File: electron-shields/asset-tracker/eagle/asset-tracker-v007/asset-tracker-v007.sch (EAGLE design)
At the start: 45 parts, among them J1 1X2-3.5MM, Q1 MPSA42, T1 DMG3415, U1 MAX-M8, U3 LIS3DHTR, U4 RF_SWITCHSC-70-6, U5 SAFFB1G56KB0F0A, U6 BGA725L6-ALT, X1 ELECTRON, X2 IPEX-20279-001E

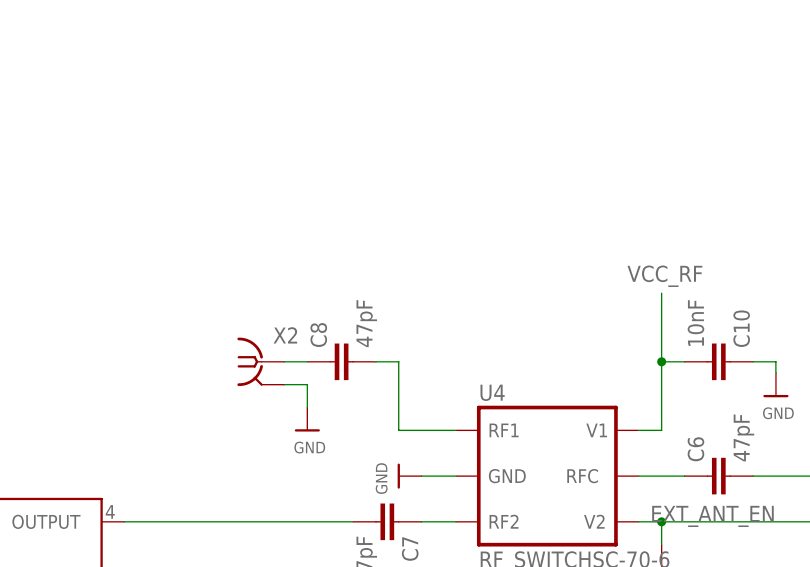
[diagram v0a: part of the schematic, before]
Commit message: added bias supply to the active antenna rf trace
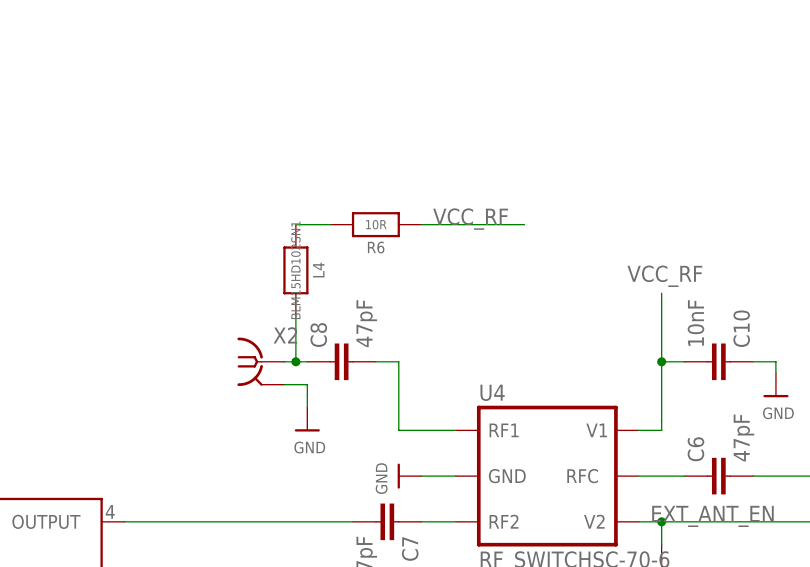
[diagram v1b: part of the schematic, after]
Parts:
- added L4: BLM15HD102SN1, microbuilder:RESISTOR_0402MP
- added R6: 10R, microbuilder:RESISTOR_0402MP
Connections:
- new net N$1: L4.1, R6.2
- net EXT_ANT: now also L4.2
- net VCC_RF: now also R6.1
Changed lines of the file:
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@@
 <setting verticaltext="up"/>
 </settings>
-<grid distance="0.1" unitdist="inch" unit="inch" style="lines" multiple="1" display="no" altdistance="0.01" altunitdist="inch" altunit="inch"/>
+<grid distance="0.05" unitdist="inch" unit="inch" style="lines" multiple="1" display="yes" altdistance="0.01" altunitdist="inch" altunit="inch"/>
 <layers>
-<layer number="1" name="Top" color="4" fill="1" visible="no" active="no"/>
-<layer number="2" name="Route2" color="5" fill="1" visible="no" active="no"/>
-<layer number="3" name="Route3" color="4" fill="3" visible="no" active="no"/>
-<layer number="4" name="Route4" color="1" fill="4" visible="no" active="no"/>
-<layer number="5" name="Route5" color="4" fill="4" visible="no" active="no"/>
-<layer number="6" name="Route6" color="1" fill="8" visible="no" active="no"/>
-<layer number="7" name="Route7" color="4" fill="8" visible="no" active="no"/>
-<layer number="8" name="Route8" color="1" fill="2" visible="no" active="no"/>
-<layer number="9" name="Route9" color="4" fill="2" visible="no" active="no"/>
-<layer number="10" name="Route10" color="1" fill="7" visible="no" active="no"/>
-<layer number="11" name="Route11" color="4" fill="7" visible="no" active="no"/>
-<layer number="12" name="Route12" color="1" fill="5" visible="no" active="no"/>
-<layer number="13" name="Route13" color="4" fill="5" visible="no" active="no"/>
-<layer number="14" name="Route14" color="1" fill="6" visible="no" active="no"/>
-<layer number="15" name="Route15" color="11" fill="1" visible="no" active="no"/>
-<layer number="16" name="Bottom" color="1" fill="1" visible="no" active="no"/>
-<layer number="17" name="Pads" color="2" fill="1" visible="no" active="no"/>
-<layer number="18" name="Vias" color="2" fill="1" visible="no" active="no"/>
-<layer number="19" name="Unrouted" color="6" fill="1" visible="no" active="no"/>
-<layer number="20" name="Dimension" color="15" fill="1" visible="no" active="no"/>
-<layer number="21" name="tPlace" color="16" fill="1" visible="no" active="no"/>
-<layer number="22" name="bPlace" color="14" fill="1" visible="no" active="no"/>
-<layer number="23" name="tOrigins" color="15" fill="1" visible="no" active="no"/>
-<layer number="24" name="bOrigins" color="15" fill="1" visible="no" active="no"/>
-<layer number="25" name="tNames" color="7" fill="1" visible="no" active="no"/>
-<layer number="26" name="bNames" color="7" fill="1" visible="no" active="no"/>
-<layer number="27" name="tValues" color="7" fill="1" visible="no" active="no"/>
-<layer number="28" name="bValues" color="7" fill="1" visible="no" active="no"/>
+<layer number="1" name="Top" color="4" fill="1" visible="yes" active="no"/>
+<layer number="2" name="Route2" color="5" fill="1" visible="yes" active="no"/>
+<layer number="3" name="Route3" color="4" fill="3" visible="yes" active="no"/>
+<layer number="4" name="Route4" color="1" fill="4" visible="yes" active="no"/>
+<layer number="5" name="Route5" color="4" fill="4" visible="yes" active="no"/>
+<layer number="6" name="Route6" color="1" fill="8" visible="yes" active="no"/>
+<layer number="7" name="Route7" color="4" fill="8" visible="yes" active="no"/>
+<layer number="8" name="Route8" color="1" fill="2" visible="yes" active="no"/>
+<layer number="9" name="Route9" color="4" fill="2" visible="yes" active="no"/>
+<layer number="10" name="Route10" color="1" fill="7" visible="yes" active="no"/>
+<layer number="11" name="Route11" color="4" fill="7" visible="yes" active="no"/>
+<layer number="12" name="Route12" color="1" fill="5" visible="yes" active="no"/>
+<layer number="13" name="Route13" color="4" fill="5" visible="yes" active="no"/>
+<layer number="14" name="Route14" color="1" fill="6" visible="yes" active="no"/>
+<layer number="15" name="Route15" color="11" fill="1" visible="yes" active="no"/>
+<layer number="16" name="Bottom" color="1" fill="1" visible="yes" active="no"/>
+<layer number="17" name="Pads" color="2" fill="1" visible="yes" active="no"/>
+<layer number="18" name="Vias" color="2" fill="1" visible="yes" active="no"/>
+<layer number="19" name="Unrouted" color="6" fill="1" visible="yes" active="no"/>
+<layer number="20" name="Dimension" color="15" fill="1" visible="yes" active="no"/>
+<layer number="21" name="tPlace" color="16" fill="1" visible="yes" active="no"/>
+<layer number="22" name="bPlace" color="14" fill="1" visible="yes" active="no"/>
+<layer number="23" name="tOrigins" color="15" fill="1" visible="yes" active="no"/>
+<layer number="24" name="bOrigins" color="15" fill="1" visible="yes" active="no"/>
+<layer number="25" name="tNames" color="7" fill="1" visible="yes" active="no"/>
+<layer number="26" name="bNames" color="7" fill="1" visible="yes" active="no"/>
+<layer number="27" name="tValues" color="7" fill="1" visible="yes" active="no"/>
+<layer number="28" name="bValues" color="7" fill="1" visible="yes" active="no"/>
 <layer number="29" name="tStop" color="32" fill="3" visible="no" active="no"/>
 <layer number="30" name="bStop" color="7" fill="6" visible="no" active="no"/>
@@
 <layer number="35" name="tGlue" color="7" fill="4" visible="no" active="no"/>
 <layer number="36" name="bGlue" color="7" fill="5" visible="no" active="no"/>
-<layer number="37" name="tTest" color="7" fill="1" visible="no" active="no"/>
-<layer number="38" name="bTest" color="7" fill="1" visible="no" active="no"/>
+<layer number="37" name="tTest" color="7" fill="1" visible="yes" active="no"/>
+<layer number="38" name="bTest" color="7" fill="1" visible="yes" active="no"/>
 <layer number="39" name="tKeepout" color="4" fill="11" visible="no" active="no"/>
 <layer number="40" name="bKeepout" color="1" fill="11" visible="no" active="no"/>
@@
 <layer number="44" name="Drills" color="7" fill="1" visible="no" active="no"/>
 <layer number="45" name="Holes" color="7" fill="1" visible="no" active="no"/>
-<layer number="46" name="Milling" color="3" fill="1" visible="no" active="no"/>
-<layer number="47" name="Measures" color="7" fill="1" visible="no" active="no"/>
-<layer number="48" name="Document" color="18" fill="1" visible="no" active="no"/>
-<layer number="49" name="Reference" color="17" fill="6" visible="no" active="no"/>
-<layer number="50" name="dxf" color="7" fill="1" visible="no" active="no"/>
-<layer number="51" name="tDocu" color="6" fill="1" visible="no" active="no"/>
-<layer number="52" name="bDocu" color="7" fill="1" visible="no" active="no"/>
-<layer number="53" name="tGND_GNDA" color="7" fill="9" visible="no" active="no"/>
-<layer number="54" name="bGND_GNDA" color="1" fill="9" visible="no" active="no"/>
-<layer number="56" name="wert" color="7" fill="1" visible="no" active="no"/>
-<layer number="57" name="tCAD" color="7" fill="1" visible="no" active="no"/>
-<layer number="59" name="tCarbon" color="7" fill="1" visible="no" active="no"/>
-<layer number="60" name="bCarbon" color="7" fill="1" visible="no" active="no"/>
+<layer number="46" name="Milling" color="3" fill="1" visible="yes" active="no"/>
+<layer number="47" name="Measures" color="7" fill="1" visible="yes" active="no"/>
+<layer number="48" name="Document" color="18" fill="1" visible="yes" active="no"/>
+<layer number="49" name="Reference" color="17" fill="6" visible="yes" active="no"/>
+<layer number="50" name="dxf" color="7" fill="1" visible="yes" active="no"/>
+<layer number="51" name="tDocu" color="6" fill="1" visible="yes" active="no"/>
+<layer number="52" name="bDocu" color="7" fill="1" visible="yes" active="no"/>
+<layer number="53" name="tGND_GNDA" color="7" fill="9" visible="yes" active="no"/>
+<layer number="54" name="bGND_GNDA" color="1" fill="9" visible="yes" active="no"/>
+<layer number="56" name="wert" color="7" fill="1" visible="yes" active="no"/>
+<layer number="57" name="tCAD" color="7" fill="1" visible="yes" active="no"/>
+<layer number="59" name="tCarbon" color="7" fill="1" visible="yes" active="no"/>
+<layer number="60" name="bCarbon" color="7" fill="1" visible="yes" active="no"/>
 <layer number="90" name="Modules" color="5" fill="1" visible="no" active="yes"/>
 <layer number="91" name="Nets" color="2" fill="1" visible="yes" active="yes"/>
@@
 <part name="C11" library="rcl" deviceset="C-EU" device="C0402" value="10nF"/>
 <part name="U$31" library="Spark" deviceset="SPARK_LOGO" device=""/>
+<part name="R6" library="microbuilder" deviceset="RESISTOR" device="_0402MP" value="10R"/>
+<part name="L4" library="microbuilder" deviceset="RESISTOR" device="_0402MP" value="BLM15HD102SN1"/>
 </parts>
 <sheets>
@@
 <instance part="C11" gate="G$1" x="273.05" y="218.44" rot="R90"/>
 <instance part="U$31" gate="G$1" x="289.56" y="25.4"/>
+<instance part="R6" gate="G$1" x="165.1" y="209.55" rot="R180"/>
+<instance part="L4" gate="G$1" x="156.21" y="204.47" rot="R270"/>
 </instances>
 <busses>
@@
 <wire x1="58.42" y1="166.37" x2="41.91" y2="166.37" width="0.1524" layer="91"/>
 <label x="41.91" y="166.37" size="1.778" layer="95"/>
+</segment>
+<segment>
+<pinref part="R6" gate="G$1" pin="1"/>
+<wire x1="170.18" y1="209.55" x2="181.61" y2="209.55" width="0.1524" layer="91"/>
+<label x="171.45" y="209.55" size="1.778" layer="95"/>
 </segment>
 </net>
@@
 <pinref part="X2" gate="G$1" pin="1"/>
 <pinref part="C8" gate="G$1" pin="1"/>
-<wire x1="157.48" y1="194.31" x2="154.94" y2="194.31" width="0.1524" layer="91"/>
+<wire x1="157.48" y1="194.31" x2="156.21" y2="194.31" width="0.1524" layer="91"/>
+<pinref part="L4" gate="G$1" pin="2"/>
+<wire x1="156.21" y1="194.31" x2="154.94" y2="194.31" width="0.1524" layer="91"/>
+<wire x1="156.21" y1="199.39" x2="156.21" y2="194.31" width="0.1524" layer="91"/>
+<junction x="156.21" y="194.31"/>
 </segment>
 </net>
@@
 </segment>
 </net>
+<net name="N$1" class="0">
+<segment>
+<pinref part="R6" gate="G$1" pin="2"/>
+<wire x1="160.02" y1="209.55" x2="156.21" y2="209.55" width="0.1524" layer="91"/>
+<pinref part="L4" gate="G$1" pin="1"/>
+</segment>
+</net>
